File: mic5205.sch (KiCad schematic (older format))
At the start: 4 parts, among them U7 MIC5205

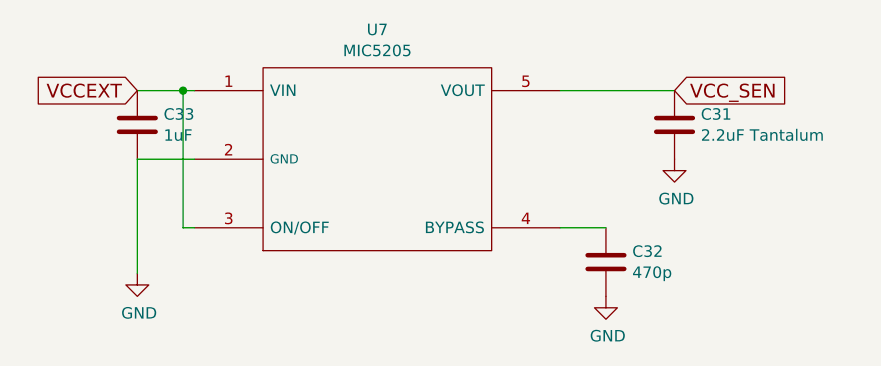
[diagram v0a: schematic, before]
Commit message: changed some netnames
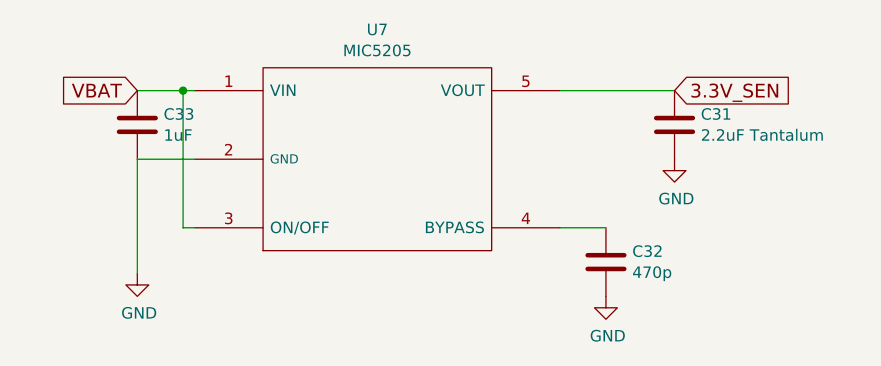
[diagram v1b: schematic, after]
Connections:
- net VCCEXT renamed VBAT
- net VCC_SEN renamed 3.3V_SEN
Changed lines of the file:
@@
 	4750 3800 4750 4300
 Text GLabel 7100 3500 2    60   Input ~ 0
-VCC_SEN
+3.3V_SEN
 Text GLabel 4750 3500 0    60   Input ~ 0
-VCCEXT
+VBAT
 $Comp
 L C C33
